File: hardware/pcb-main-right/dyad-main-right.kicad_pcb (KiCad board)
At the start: 2 copper layers, 167.2 x 120.7 mm, 148 parts, among them SW1 SW_Push, SW10 SW_Push, SW11 SW_Push, SW12 SW_Push, SW13 SW_Push, SW14 SW_Push, SW15 SW_Push, SW16 SW_Push, SW17 SW_Push, SW18 SW_Push, SW19 SW_Push, SW2 SW_Push, SW20 SW_Push, SW21 SW_Push, SW22 SW_Push, SW23 SW_Push, SW24 SW_Push, SW25 SW_Push, SW26 SW_Push, SW27 SW_Push, SW28 SW_Push, SW29 SW_Push, SW3 SW_Push, SW30 SW_Push, SW31 SW_Push, SW32 SW_Push, SW33 SW_Push, SW34 SW_Push, SW35 SW_Push, SW36 SW_Push, SW37 SW_Push, SW4 SW_Push, SW5 SW_Push, SW6 SW_Push, SW7 SW_Push, SW8 SW_Push, SW9 SW_Push

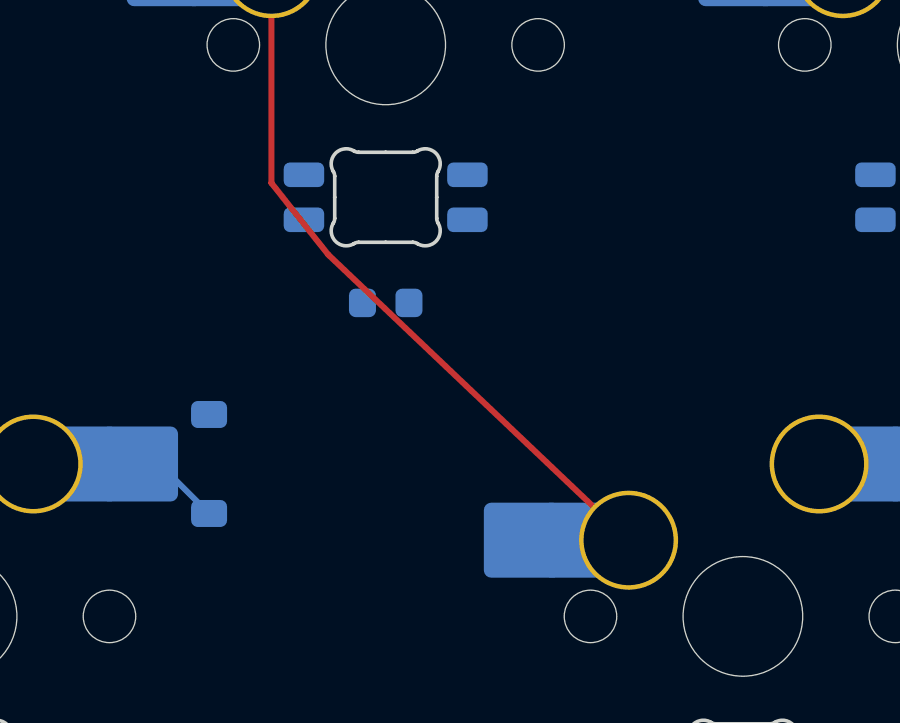
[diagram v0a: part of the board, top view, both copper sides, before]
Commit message: Regenerate both main PCBs with hierarchical sheet bundling
Re-ran generate_main_pcbs.py so the --bundle-strategy hierarchical change
takes effect. Each half now has a proper root sheet:

  dyad-main-<half>.kicad_sch             0 symbols, 2 child sheet refs
  dyad-main-<half>-key-matrix.kicad_sch  65 / 74 symbols   (new file)
  dyad-main-<half>-led-chain.kicad_sch   130 / 150 symbols

The key-matrix sheet is new: flat bundling put those symbols in the root
itself, hierarchical moves them into their own child sheet.

Schematic parity is the point of the exercise:

              before              after
  main-left   64 Extra footprint  0
  main-right  74 Extra footprint  0

Every LED and decoupling capacitor now resolves to a symbol. The parity
counts happen to be unchanged (98 and 111) but the composition is entirely
different -- what remains is cosmetic field sync (Sim.Device, Description
and Datasheet empty on the PCB side), not missing structure.

min_copper_edge_clearance is 0.2 on both, so _relax_edge_clearance ran, and
the fp-lib-table files added earlier were preserved, so lib_footprint_issues
stays at zero.

Known, unchanged by this commit:
  - COL6 vs LED14's cutout is back at 0.036 mm on main-right, identical to
    before -- kbplacer re-routes it the same way every time, which is why
    the hand fix in e7043c7 was always going to be temporary.
  - The 2.25u stabilised key still falls back to a 1.0u footprint.
  - Four rotated thumb/pod pairs per half remain unrouted ("Could not route
    pads when parent footprints not rotated the same").

Co-Authored-By: Claude Opus 5 <noreply@anthropic.com>
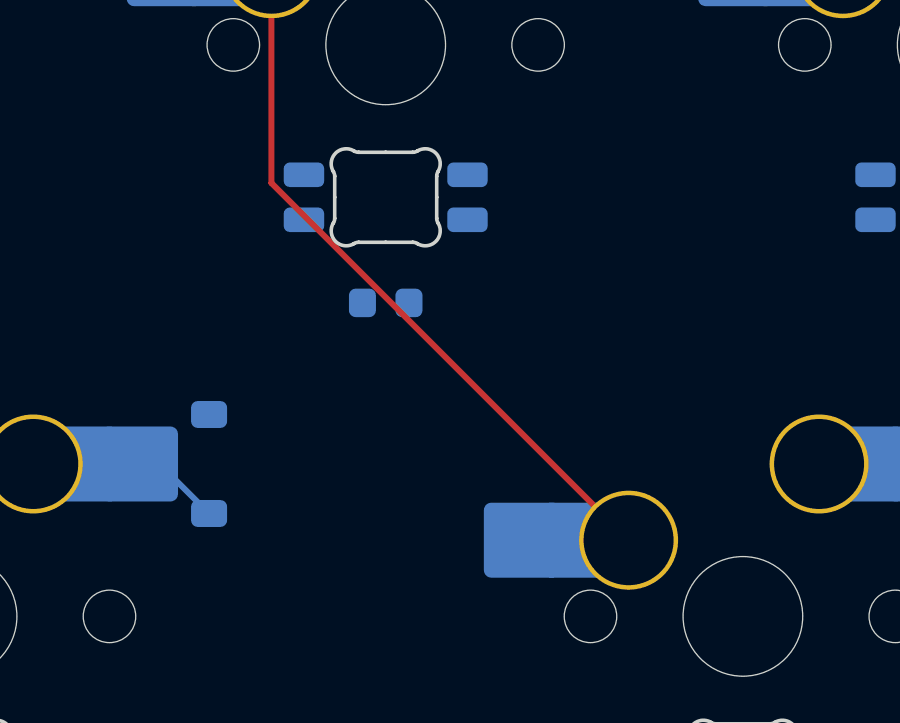
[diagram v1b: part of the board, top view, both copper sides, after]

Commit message: Bend auto-routed copper clear of the LED light cutouts
LED_SK6812MINI-E_..._ReverseMount cuts its own light hole, so the footprint
carries Edge.Cuts geometry of its own. kbplacer routes rows and columns
without seeing those holes, and on the right half COL6 lands 0.036 mm from
LED14's cutout against the 0.2 mm rule -- close enough that the routing slot
could sever the trace. It reproduces byte-identically on every run, so the
hand fix in e7043c7 was erased by the very next regeneration.

_nudge_traces_off_led_cutouts() now runs as a post-processing pass, in the
same spirit as _propagate_pad_nets. For every copper track that collides
with a footprint-internal Edge.Cuts shape it splits the track at a waypoint
pushed away from the hole, trying 0.35 mm and widening to 1.5 mm until the
geometry clears. Endpoints never move, so pad connections and the joins to
neighbouring segments are preserved. Candidate waypoints are proven against
a throwaway probe track before the board is touched, a split is refused when
the closest approach is within 5% of either end (it would leave a stub), and
anything unresolvable is reported for hand routing rather than mangled.

Collision detection is KiCad's own SHAPE::Collide rather than hand geometry.
On main-right it selects exactly the one track DRC reports, out of 114 tracks
against 740 footprint cutouts -- no false positives.

The 0.2 mm figure is now the module-level EDGE_CLEARANCE_MM, shared with
_relax_edge_clearance so the rule the pass satisfies and the rule written
into the project cannot drift apart.

Boards regenerated with the pass in place:

               nudged  non-courtyard errors  unconnected  Extra footprint
  main-left         0                     0          188                0
  main-right        1                     0          223                0

Every remaining error on both halves is a deliberate D/SW courtyard overlap
from the diode-under-switch placement. Unconnected counts are unchanged, so
nothing was disco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
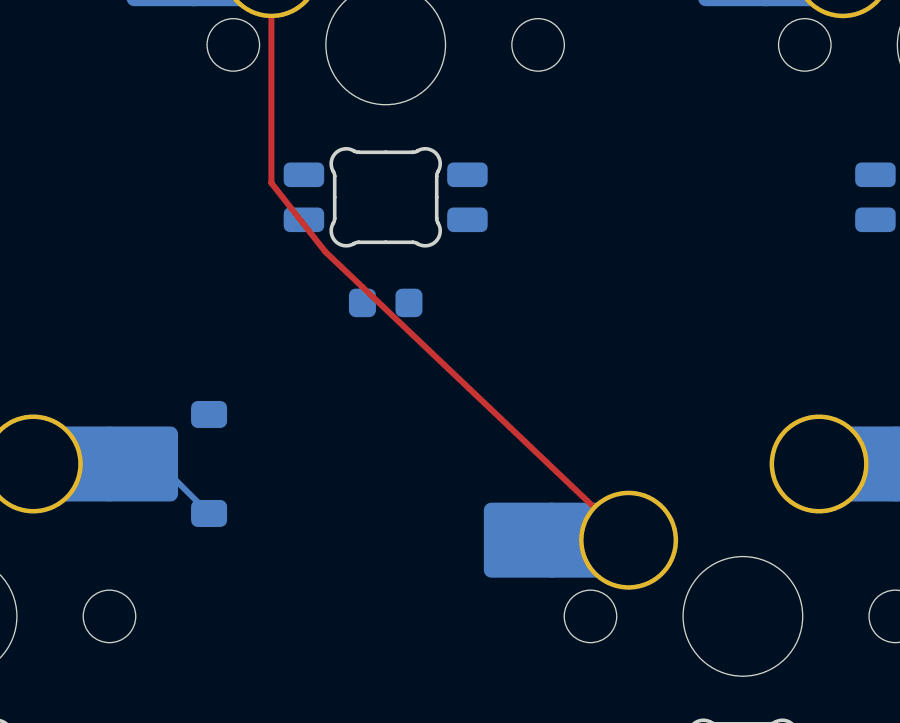
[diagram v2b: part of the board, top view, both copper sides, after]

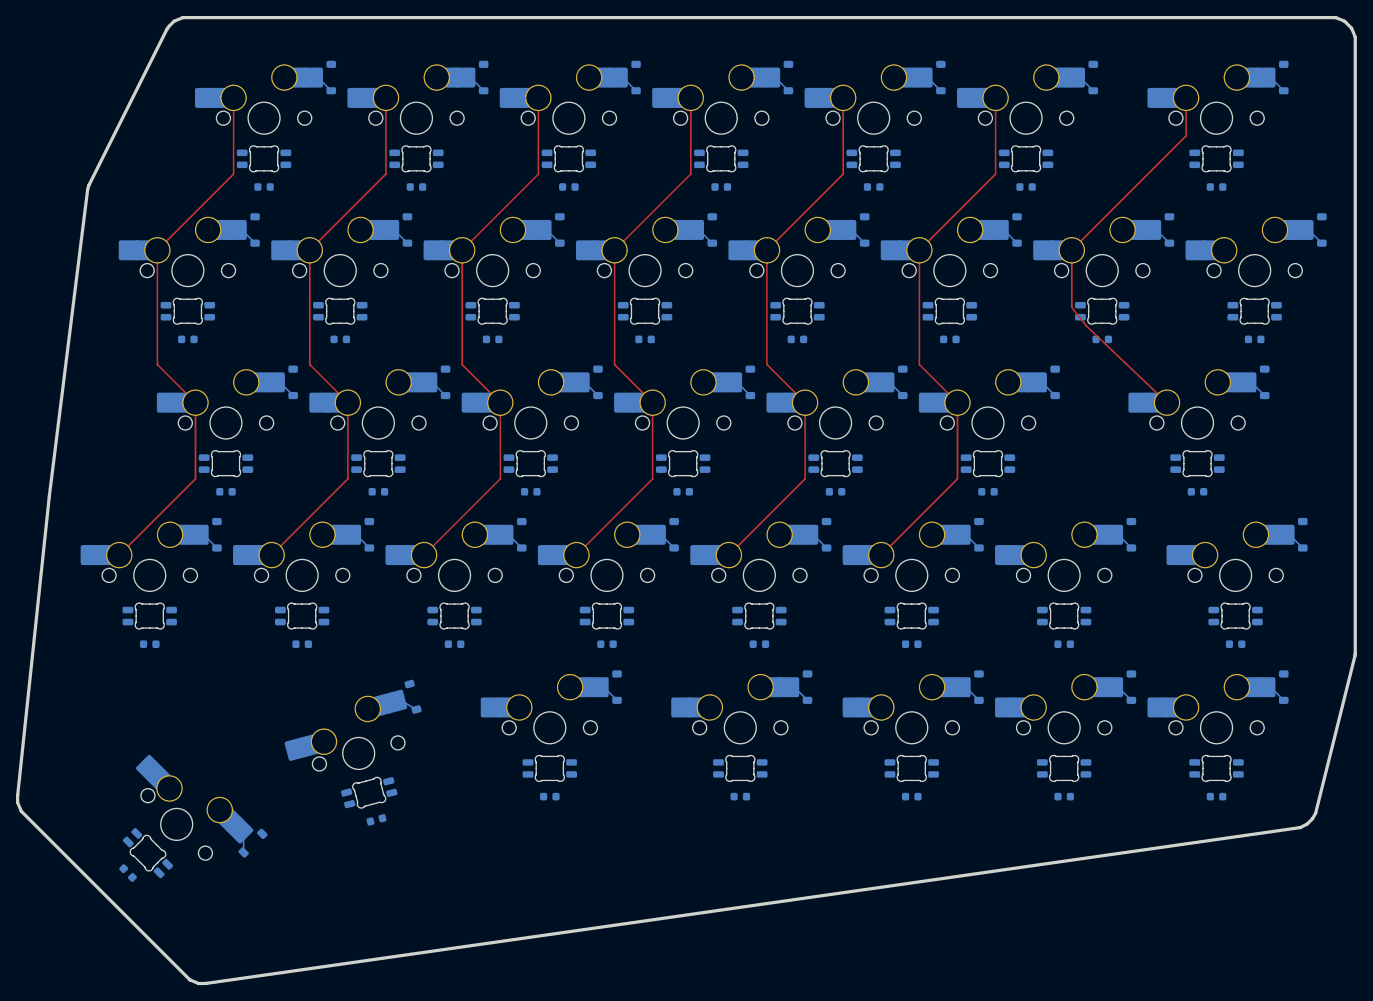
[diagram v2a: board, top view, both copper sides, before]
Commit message: Move the right half's thumb keys onto their physical columns, and route it
The two rotated thumb keys were wired to COL5 and COL6 while sitting
physically leftmost on the board, because KLE puts rotated keys in their own
rows and they were numbered last. COL5 and COL6 therefore had to reach ~92 mm
across the board to find them. Relabelled 4,5 -> 4,0 and 4,6 -> 4,1 in the
KLE (with the five straight bottom-row keys shifted up to 4,2..4,6 to make
room) and regenerated: SW31 is now COL0 at x=46.23 and SW32 is COL1 at
x=68.98, both directly below the columns they belong to.

Also carries the hand routing done on top of that regeneration: all five ROW
nets and COL0-COL5, COL7 complete, 118 -> 234 segments. Unconnected 221 -> 183.
The remainder is 146 VCC/GND (no copper pours yet), 36 LED DOUT chain, and one
COL6 hop from SW22's pad to the end of its track.

Two errors on COL3 predate the routing and come from kbplacer's generated
traces: 0.1386 mm to LED26's cutout, and 0.197 mm to SW26's NPTH pad. The
nudge pass declined the first rather than mangle it -- it treats each
Edge.Cuts primitive as a separate obstacle and pushes away from that
primitive's bounding-box centre, which is meaningless for the 0.12 mm slivers
this cutout is built from. Grouping a footprint's Edge.Cuts into one obstacle
would fix it.

Co-Authored-By: Claude Opus 5 <noreply@anthropic.com>
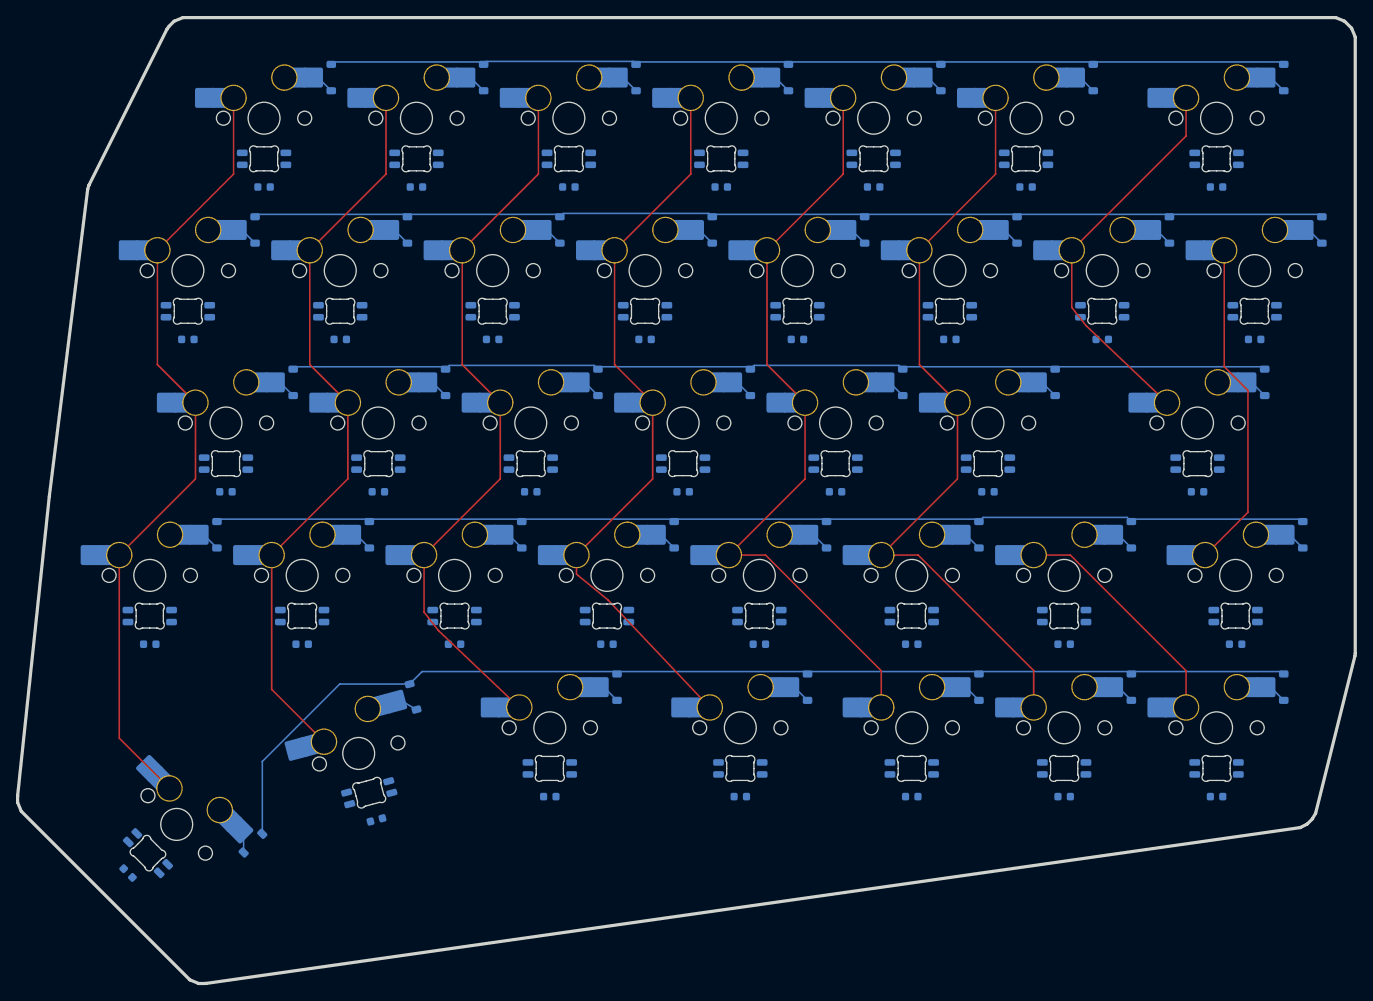
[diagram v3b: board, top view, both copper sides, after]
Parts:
- SW31: footprint marbastlib-mx:SW_MX_HS_CPG151101S11_1.25u -> marbastlib-mx:SW_MX_HS_CPG151101S11_1.5u
- SW32: footprint marbastlib-mx:SW_MX_HS_CPG151101S11_1.25u -> marbastlib-mx:SW_MX_HS_CPG151101S11_1u
- SW33, SW34: footprint marbastlib-mx:SW_MX_HS_CPG151101S11_1u -> marbastlib-mx:SW_MX_HS_CPG151101S11_1.25u
- SW36: footprint marbastlib-mx:SW_MX_HS_CPG151101S11_1.5u -> marbastlib-mx:SW_MX_HS_CPG151101S11_1u
- moved C36 117.4 mm to (157.2, 122.9), turned to 180 degrees
- moved LED36 115.0 mm to (157.2, 119.4), turned to 180 degrees
- moved SW36 111.6 mm to (157.2, 114.3), turned to 180 degrees
- moved D36 111.5 mm to (165.6, 109.2), turned to -90 degrees
- moved D37 108.8 mm to (184.6, 109.2), turned to -90 degrees
- moved SW37 107.3 mm to (176.2, 114.3), turned to 180 degrees
- moved LED37 106.0 mm to (176.2, 119.4), turned to 180 degrees
- moved C37 105.0 mm to (176.2, 122.9), turned to 180 degrees
- moved C31 53.6 mm to (40.1, 132.5), turned to 135 degrees
- moved LED31 51.3 mm to (42.6, 130.0), turned to 135 degrees
- moved D31 49.5 mm to (55.8, 128.7), turned to -135 degrees
- moved D32 49.3 mm to (75.8, 110.4), turned to -75 degrees
- moved SW31 48.2 mm to (46.2, 126.4), turned to 135 degrees
- moved SW32 47.8 mm to (69.0, 117.5), turned to -165 degrees
- moved LED32 46.5 mm to (70.3, 122.4), turned to -165 degrees
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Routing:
- net ROW4: track 0.00 -> 142.5 mm
- net ROW3: track 0.00 -> 137.7 mm
- net ROW1: track 0.00 -> 135.2 mm
- net ROW2: track 0.00 -> 123.2 mm
- net ROW0: track 0.00 -> 120.6 mm
- net COL7: track 0.00 -> 41.5 mm
- net COL0: track 67.0 -> 98.8 mm
- net COL5: track 67.0 -> 96.7 mm
- net COL6: track 49.0 -> 78.6 mm
- net COL4: track 67.0 -> 96.6 mm
- net COL1: track 67.0 -> 93.0 mm
- net COL3: track 67.0 -> 93.0 mm
- net COL2: track 67.0 -> 91.0 mm

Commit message: Pour GND and VCC from the generator, and write down what stays manual
_add_power_pours() fills one rail per layer over the real board outline,
taken from KiCad's own outline extraction rather than reassembling the 25
Edge.Cuts segments. Pads connect solid rather than through thermal reliefs:
everything here is reflow SMD, so thermal relief buys nothing and costs the
LED rail current capacity. It also sidesteps the starved_thermal class of
error entirely.

GND goes on B.Cu, the component side. Every GND pad on these boards is
B.Cu-only, so the pour reaches all of them with no vias, and each LED's
decoupling loop to its own capacitor stays local copper rather than going
pad -> via -> plane -> via -> pad. Result: GND unconnected 0 on both halves.

VCC takes F.Cu, which carries only column traces and so gives a continuous
plane for spreading ~2 A across the LEDs. It cannot reach its pads without a
via each, and those are being added by hand -- documented rather than
generated, since via placement wants judgement about the LED/cap pairs.

  main-left    GND 12918 mm2   VCC 13646 mm2
  main-right   GND 14088 mm2   VCC 14924 mm2

Both halves regenerated, which also applies the pending bottom-row column
remap from 9b392c8. That resolved the two COL3 errors on the right -- the
0.1386 mm to LED26's cutout and 0.197 mm to SW26's NPTH pad both came from
routing that no longer exists. Every remaining error on both halves is now a
deliberate D/SW courtyard overlap.

docs/MANUAL_TASKS.md records the four things the generator cannot do: the VCC
vias, routing the rows and columns, the LED serpentine chain, and the
cosmetic silkscreen work. It carries the post-regeneration baseline numbers so
an anomaly is distinguishable from a known gap, and a "do not fix" section for
the courtyard overlaps and the 2.25u width fallback, both of which have now
been investigated twice.

Co-Authored-By: Claude Opus 5 <noreply@anthropic.com>
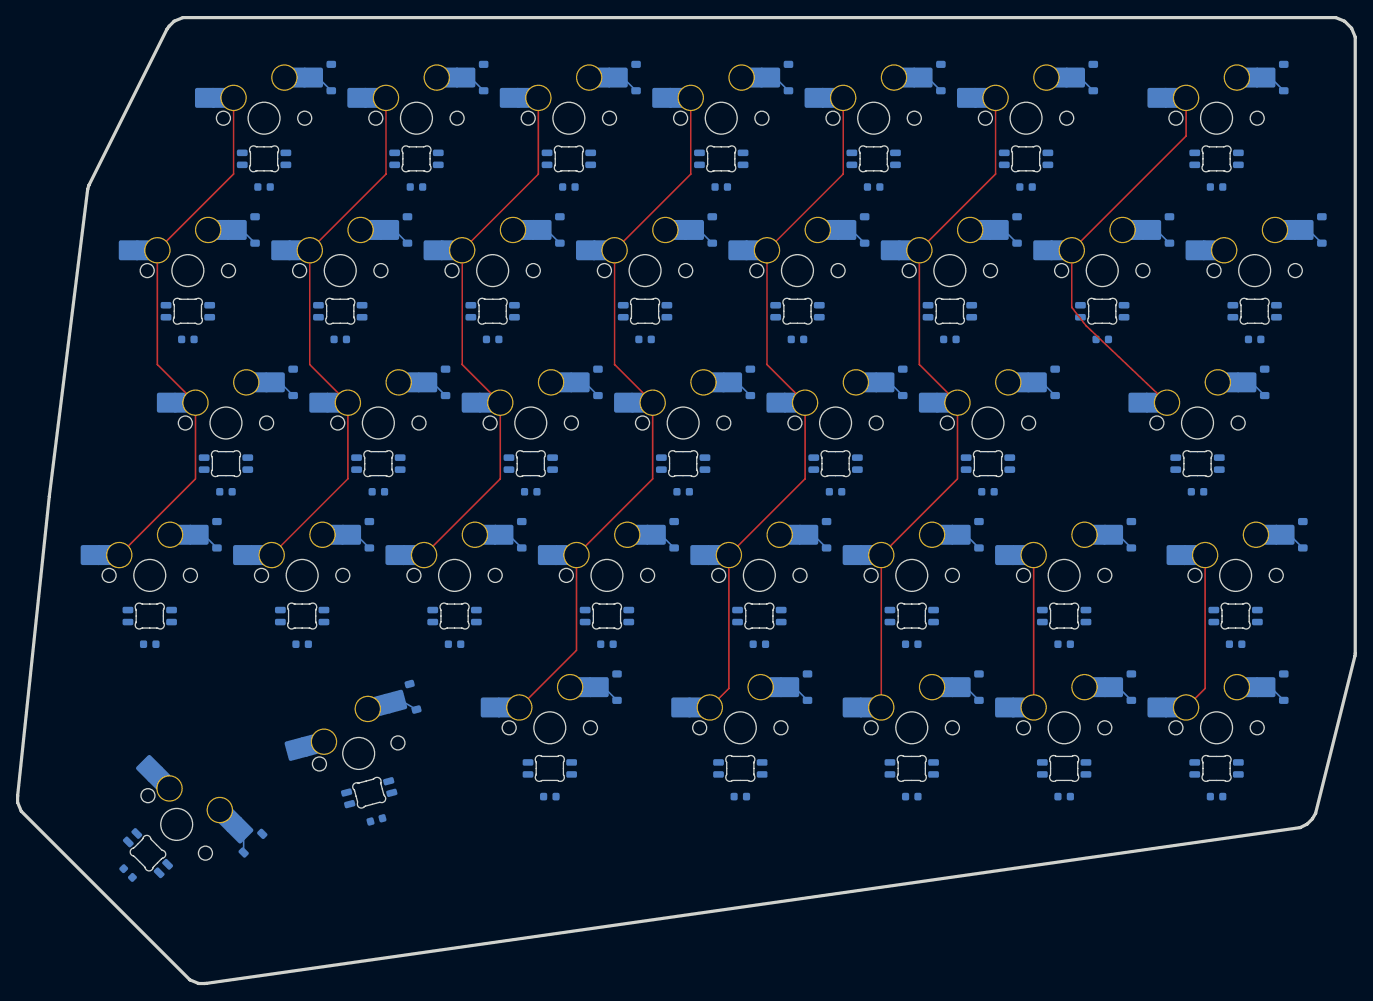
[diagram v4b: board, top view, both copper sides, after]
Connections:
- SW33 pad 1: COL2 -> COL3
- SW34 pad 1: COL3 -> COL4
- SW35 pad 1: COL4 -> COL5
- SW36 pad 1: COL5 -> COL6
- SW37 pad 1: COL6 -> COL7
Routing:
- net ROW4: track 142.5 -> 0.00 mm
- net ROW3: track 137.7 -> 0.00 mm
- net ROW1: track 135.2 -> 0.00 mm
- net ROW2: track 123.2 -> 0.00 mm
- net ROW0: track 120.6 -> 0.00 mm
- net COL0: track 98.8 -> 67.0 mm
- net COL1: track 93.0 -> 67.0 mm
- net COL2: track 91.0 -> 67.0 mm
- net COL7: track 41.5 -> 20.0 mm
- net COL5: track 96.7 -> 86.1 mm
- net COL6: track 78.6 -> 68.0 mm
- net COL4: track 96.6 -> 87.0 mm
- net COL3: track 93.0 -> 89.0 mm
- added copper zone on B.Cu, net GND
- added copper zone on F.Cu, net VCC
